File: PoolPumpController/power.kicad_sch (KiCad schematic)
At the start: 12 parts, among them U1 LS05-13B05R3

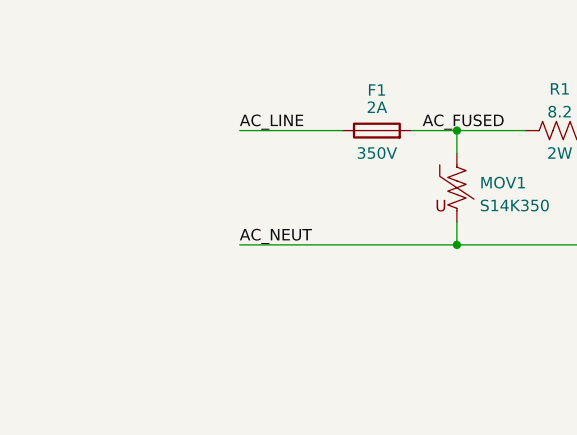
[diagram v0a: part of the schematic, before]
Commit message: Changed screw terminal symbols used for power connections to test points that will be used for soldering wires from a panel mount connector.
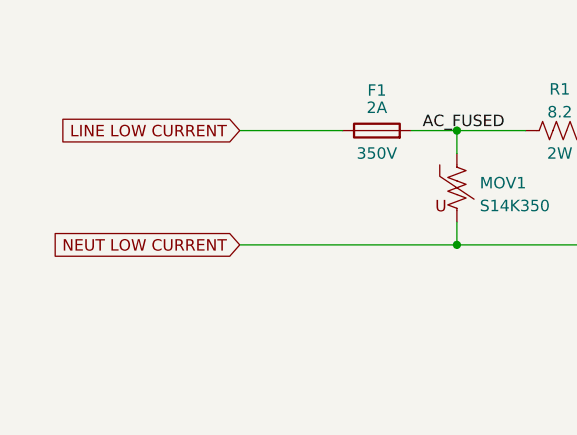
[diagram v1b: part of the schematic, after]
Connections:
- net AC_LINE renamed LINE LOW CURRENT
- net AC_NEUT renamed NEUT LOW CURRENT
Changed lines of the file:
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@@
-    (effects (font (size 1.27 1.27)) (justify left bottom))
-  )
-  (label "AC_LINE" (at 72.39 83.82 0)
     (effects (font (size 1.27 1.27)) (justify left bottom))
   )
@@
     (effects (font (size 1.27 1.27)) (justify left bottom))
   )
-  (label "AC_NEUT" (at 72.39 96.52 0)
-    (effects (font (size 1.27 1.27)) (justify left bottom))
-  )
   (label "DC_FILT-" (at 125.73 107.95 0)
     (effects (font (size 1.27 1.27)) (justify left bottom))
   )
+  (global_label "NEUT LOW CURRENT" (shape input) (at 72.39 96.52 180) (fields_autoplaced)
+    (effects (font (size 1.27 1.27)) (justify right))
+    (property "Intersheet References" "${INTERSHEET_REFS}" (id 0) (at 50.8664 96.4406 0)
+      (effects (font (size 1.27 1.27)) (justify right) hide)
+    )
+  )
+  (global_label "LINE LOW CURRENT" (shape input) (at 72.39 83.82 180) (fields_autoplaced)
+    (effects (font (size 1.27 1.27)) (justify right))
+    (property "Intersheet References" "${INTERSHEET_REFS}" (id 0) (at 51.5317 83.7406 0)
+      (effects (font (size 1.27 1.27)) (justify right) hide)
+    )
+  )
   (symbol (lib_id "Device:L") (at 120.65 83.82 90) (unit 1)
